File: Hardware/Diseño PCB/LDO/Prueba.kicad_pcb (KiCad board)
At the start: 2 copper layers, 54 parts, among them Q1 2N3904, Q10 BC557, Q11 BC547, Q12 BC557, Q13 2N3906, Q14 2N3904, Q15 2N3906, Q16 2N3904, Q17 2N3906, Q18 2N3904, Q19 2N3904, Q2 2N3904, Q3 2N3904, Q4 2N3906, Q5 2N3906, Q6 2N3904, Q7 2N3904, Q8 IRF4905, Q9 BC547, U1 TL431LP, U4 LM324

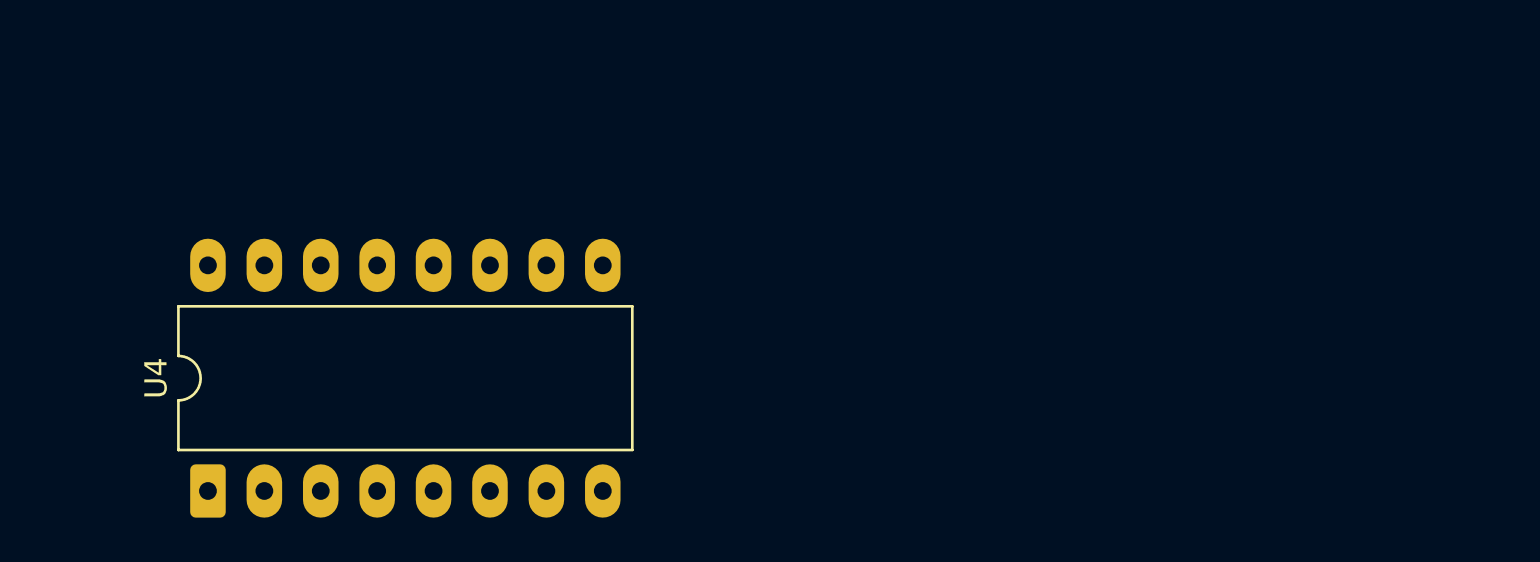
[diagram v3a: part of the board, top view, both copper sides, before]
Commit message: Diseño PCB:Arreglo LM324s con 14 pines
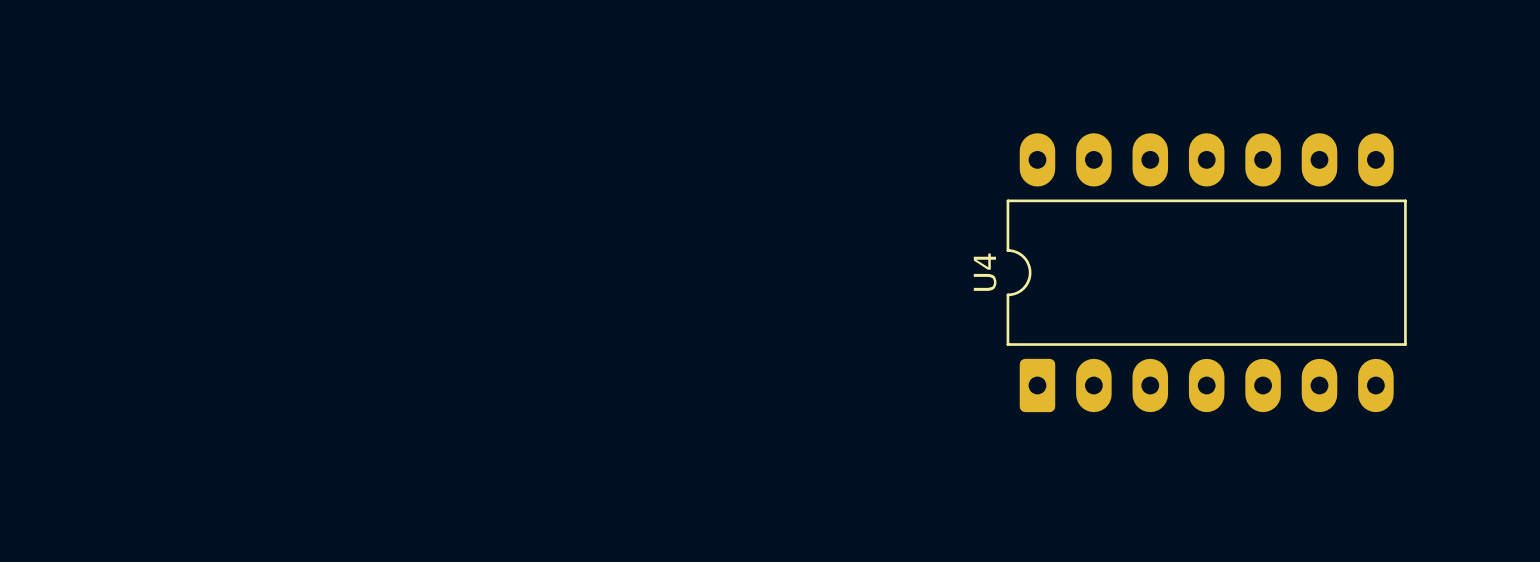
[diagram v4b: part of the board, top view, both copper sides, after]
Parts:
- U4: footprint Package_DIP:DIP-16_W10.16mm_LongPads -> Package_DIP:DIP-14_W10.16mm_LongPads
- moved U4 37.7 mm to (192.6, 102.9)
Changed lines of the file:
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@@
 		)
 	)
-	(footprint "Package_DIP:DIP-16_W10.16mm_LongPads"
+	(footprint "Package_DIP:DIP-14_W10.16mm_LongPads"
 		(layer "F.Cu")
-		(at 155.22 107.66 90)
-		(descr "16-lead though-hole mounted DIP package, row spacing 10.16mm (400 mils), LongPads")
+		(at 192.575412 102.909815 90)
+		(descr "14-lead though-hole mounted DIP package, row spacing 10.16mm (400 mils), LongPads")
 		(tags "THT DIP DIL PDIP 2.54mm 10.16mm 400mil LongPads")
 		(property "Reference" "U4"
@@
 		)
 		(property "Value" "LM324"
-			(at 5.08 20.11 90)
+			(at 5.08 17.57 90)
 			(layer "F.Fab")
 			(effects
@@
 		(fp_line
 			(start 1.845 -1.33)
-			(end 1.845 19.11)
+			(end 1.845 16.57)
 			(stroke
 				(width 0.12)
@@
 		)
 		(fp_line
-			(start 8.315 19.11)
+			(start 8.315 16.57)
 			(end 8.315 -1.33)
 			(stroke
@@
 		)
 		(fp_line
-			(start 1.845 19.11)
-			(end 8.315 19.11)
+			(start 1.845 16.57)
+			(end 8.315 16.57)
 			(stroke
 				(width 0.12)
@@
 		)
 		(fp_rect
-			(start -1.46 -1.52)
-			(end 11.61 19.3)
+			(start -1.46 -1.53)
+			(end 11.61 16.77)
 			(stroke
 				(width 0.05)
@@
 		(fp_line
 			(start 8.255 -1.27)
-			(end 8.255 19.05)
+			(end 8.255 16.51)
 			(stroke
 				(width 0.1)
@@
 		)
 		(fp_line
-			(start 8.255 19.05)
-			(end 1.905 19.05)
+			(start 8.255 16.51)
+			(end 1.905 16.51)
 			(stroke
 				(width 0.1)
@@
 		)
 		(fp_line
-			(start 1.905 19.05)
+			(start 1.905 16.51)
 			(end 1.905 -0.27)
 			(stroke
@@
 		)
 		(fp_text user "${REFERENCE}"
-			(at 5.08 8.89 0)
+			(at 5.08 7.62 180)
 			(layer "F.Fab")
 			(effects
@@
 		)
 		(point
-			(at 164.11 102.58)
+			(at 200.195412 97.829815)
 			(size 1.27)
 			(layer "F.Fab")
@@
 		)
 		(pad "8" thru_hole oval
-			(at 0 17.78 90)
+			(at 10.16 15.24 90)
 			(size 2.4 1.6)
 			(drill 0.8)
@@
 		)
 		(pad "9" thru_hole oval
-			(at 10.16 17.78 90)
+			(at 10.16 12.7 90)
 			(size 2.4 1.6)
 			(drill 0.8)
@@
 		)
 		(pad "10" thru_hole oval
-			(at 10.16 15.24 90)
+			(at 10.16 10.16 90)
 			(size 2.4 1.6)
 			(drill 0.8)
@@
 		)
 		(pad "11" thru_hole oval
-			(at 10.16 12.7 90)
+			(at 10.16 7.62 90)
 			(size 2.4 1.6)
 			(drill 0.8)
@@
 		)
 		(pad "12" thru_hole oval
-			(at 10.16 10.16 90)
+			(at 10.16 5.08 90)
 			(size 2.4 1.6)
 			(drill 0.8)
@@
 		)
 		(pad "13" thru_hole oval
-			(at 10.16 7.62 90)
+			(at 10.16 2.54 90)
 			(size 2.4 1.6)
 			(drill 0.8)
@@
 		)
 		(pad "14" thru_hole oval
-			(at 10.16 5.08 90)
+			(at 10.16 0 90)
 			(size 2.4 1.6)
 			(drill 0.8)
@@
 			(pintype "output")
 		)
-		(pad "15" thru_hole oval
-			(at 10.16 2.54 90)
-			(size 2.4 1.6)
-			(drill 0.8)
-			(layers "*.Cu" "*.Mask")
-			(remove_unused_layers no)
-		)
-		(pad "16" thru_hole oval
-			(at 10.16 0 90)
-			(size 2.4 1.6)
-			(drill 0.8)
-			(layers "*.Cu" "*.Mask")
-			(remove_unused_layers no)
-		)
 		(embedded_fonts no)
-		(model "${KICAD10_3DMODEL_DIR}/Package_DIP.3dshapes/DIP-16_W10.16mm.step"
+		(model "${KICAD10_3DMODEL_DIR}/Package_DIP.3dshapes/DIP-14_W10.16mm.step"
 			(offset
 				(xyz 0 0 0)
@@
 	(gr_poly
 		(pts
-			(xy 157.228511 105.5) (xy 158.953099 103.750185) (xy 160.728511 105.5)
+			(xy 194.275412 100.749815) (xy 196 99) (xy 197.775412 100.749815)
 		)
 		(stroke
@@
 	(gr_poly
 		(pts
-			(xy 165 105.249815) (xy 166.724588 103.5) (xy 168.5 105.249815)
+			(xy 198.275412 95) (xy 196.550824 96.749815) (xy 194.775412 95)
 		)
 		(stroke
@@
 	(gr_poly
 		(pts
-			(xy 165.724588 99.750185) (xy 164 101.5) (xy 162.224588 99.750185)
+			(xy 203.050824 100.49963) (xy 204.775412 98.749815) (xy 206.550824 100.49963)
 		)
 		(stroke
@@
 	(gr_poly
 		(pts
-			(xy 173.724588 100.250185) (xy 172 102) (xy 170.224588 100.250185)
+			(xy 206 95) (xy 204.275412 96.749815) (xy 202.5 95)
 		)
 		(stroke
@@
 		(layer "Cmts.User")
 	)
-	(gr_line
-		(start 155 103.750185)
-		(end 155 106)
+	(gr_rect
+		(start 162 62.263305)
+		(end 183 78.736694)
 		(stroke
-			(width 0.1)
-			(type default)
+			(width 0.2)
+			(type solid)
 		)
+		(fill no)
 		(layer "Cmts.User")
 	)
-	(gr_line
-		(start 158.953099 103.750185)
-		(end 155 103.750185)
+	(gr_rect
+		(start 169.509604 19.907961)
+		(end 199.351572 45.625121)
 		(stroke
-			(width 0.1)
-			(type default)
+			(width 0.2)
+			(type solid)
 		)
+		(fill no)
 		(layer "Cmts.User")
 	)
-	(gr_line
-		(start 160.5 102)
-		(end 160.5 99.5)
+	(gr_rect
+		(start 187.5 87.475256)
+		(end 224.476562 110)
 		(stroke
 			(width 0.2)
 			(type solid)
 		)
+		(fill no)
 		(layer "Cmts.User")
 	)
 	(gr_rect
-		(start 162 62.263305)
-		(end 183 78.736694)
+		(start 189 50)
+		(end 225.976562 85.024744)
 		(stroke
 			(width 0.2)
@@
 	)
 	(gr_line
-		(start 164 101.5)
-		(end 164 102)
+		(start 192.046901 99)
+		(end 192.046901 101.249815)
 		(stroke
-			(width 0.2)
-			(type solid)
+			(width 0.1)
+			(type default)
 		)
 		(layer "Cmts.User")
 	)
 	(gr_line
-		(start 164 102)
-		(end 160.5 102)
+		(start 192.275412 95.249815)
+		(end 192.275412 96.749815)
 		(stroke
-			(width 0.2)
-			(type solid)
+			(width 0.1)
+			(type default)
 		)
 		(layer "Cmts.User")
 	)
 	(gr_line
-		(start 166.724588 103.5)
-		(end 170.5 103.5)
+		(start 192.275412 96.749815)
+		(end 192.275412 95.249815)
 		(stroke
 			(width 0.1)
@@
 		(layer "Cmts.User")
 	)
-	(gr_rect
-		(start 169.509604 19.907961)
-		(end 199.351572 45.625121)
+	(gr_line
+		(start 192.275412 96.749815)
+		(end 196.550824 96.749815)
 		(stroke
-			(width 0.2)
-			(type solid)
+			(width 0.1)
+			(type default)
 		)
-		(fill no)
 		(layer "Cmts.User")
 	)
 	(gr_line
-		(start 170.5 105.5)
-		(end 170.5 103.5)
+		(start 196 99)
+		(end 192.046901 99)
 		(stroke
 			(width 0.1)
@@
 	)
 	(gr_line
-		(start 172 102)
-		(end 172 103)
+		(start 204.275412 97.249815)
+		(end 204.275412 96.749815)
 		(stroke
 			(width 0.1)
@@
 	)
 	(gr_line
-		(start 172 103)
-		(end 173 103)
+		(start 204.775412 98.749815)
+		(end 208.550824 98.749815)
 		(stroke
 			(width 0.1)
@@
 	)
 	(gr_line
-		(start 173 103)
-		(end 173 105.5)
+		(start 207.525412 97.249815)
+		(end 204.275412 97.249815)
 		(stroke
 			(width 0.1)
@@
 	)
 	(gr_line
-		(start 173 105.5)
-		(end 173 106)
+		(start 207.525412 97.249815)
+		(end 207.525412 95.249815)
 		(stroke
 			(width 0.1)
@@
 		(layer "Cmts.User")
 	)
-	(gr_rect
-		(start 189 50)
-		(end 225.976562 85.024744)
+	(gr_line
+		(start 208.550824 100.749815)
+		(end 208.550824 98.749815)
 		(stroke
-			(width 0.2)
-			(type solid)
+			(width 0.1)
+			(type default)
 		)
-		(fill no)
 		(layer "Cmts.User")
 	)
@@
 		)
 	)
-	(gr_text "Amplificadores Operacionales"
-		(at 154.5 113 0)
+	(gr_text "Lazo Tensión\n"
+		(at 166.5 74.236694 0)
 		(layer "Cmts.User")
 		(effects
@@
 		)
 	)
-	(gr_text "Lazo Tensión\n"
-		(at 166.5 74.236694 0)
+	(gr_text "Ampli. aC\n"
+		(at 171 24.5 0)
 		(layer "Cmts.User")
 		(effects
@@
 		)
 	)
-	(gr_text "Ampli. aC\n"
-		(at 171 24.5 0)
+	(gr_text "Amplificadores Operacionales"
+		(at 189.275412 108.249815 0)
 		(layer "Cmts.User")
 		(effects

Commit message: Diseño PCB
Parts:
- moved R5 91.2 mm to (84.4, 25.2)
- moved R6 91.2 mm to (84.6, 21.0)
- moved V_current_test1 66.3 mm to (109.0, 98.0)
- moved GND1 66.3 mm to (81.9, 98.0)
- moved V_Rs_test1 66.3 mm to (115.4, 98.0), turned to 180 degrees
- moved V_ref_c_test1 66.3 mm to (96.9, 97.5)
- moved V_ref_test1 66.3 mm to (90.4, 97.5)
- moved V_voltage_test1 66.3 mm to (102.4, 98.0)
- moved Q8 59.4 mm to (190.9, 40.4)
- moved U4 57.8 mm to (135.0, 97.9)
- moved Vo1 55.8 mm to (193.8, 95.8), turned to 90 degrees
- moved Q9 43.7 mm to (160.9, 69.0)
- moved Q10 43.7 mm to (152.5, 55.0)
- moved Q11 43.7 mm to (152.5, 62.0)
- moved Q12 43.7 mm to (152.5, 69.0)
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
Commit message: Diseño PCB
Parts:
- moved R2 4.05 mm to (85.0, 51.0)
- moved Q1 3.77 mm to (85.0, 46.3)
- moved R1 0.77 mm to (90.9, 41.2)
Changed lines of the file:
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@@
 	(footprint "Resistor_THT:R_Axial_DIN0204_L3.6mm_D1.6mm_P7.62mm_Horizontal"
 		(layer "F.Cu")
-		(at 90.948281 40.42 -90)
+		(at 90.948281 41.19 -90)
 		(descr "Resistor, Axial_DIN0204 series, Axial, Horizontal, pin pitch=7.62mm, 0.167W, length*diameter=3.6*1.6mm^2, http://cdn-reichelt.de/documents/datenblatt/B400/1_4W%23YAG.pdf")
 		(tags "Resistor Axial_DIN0204 series Axial Horizontal pin pitch 7.62mm 0.167W length 3.6mm diameter 1.6mm")
@@
 	(footprint "Resistor_THT:R_Axial_DIN0204_L3.6mm_D1.6mm_P7.62mm_Horizontal"
 		(layer "F.Cu")
-		(at 80.948281 51 -90)
+		(at 85 51 -90)
 		(descr "Resistor, Axial_DIN0204 series, Axial, Horizontal, pin pitch=7.62mm, 0.167W, length*diameter=3.6*1.6mm^2, http://cdn-reichelt.de/documents/datenblatt/B400/1_4W%23YAG.pdf")
 		(tags "Resistor Axial_DIN0204 series Axial Horizontal pin pitch 7.62mm 0.167W length 3.6mm diameter 1.6mm")
@@
 	(footprint "Package_TO_SOT_THT:TO-92_Inline"
 		(layer "F.Cu")
-		(at 81.308281 45.5 90)
+		(at 85 46.27 90)
 		(descr "TO-92 leads in-line, narrow, oval pads, drill 0.75mm (see NXP sot054_po.pdf)")
 		(tags "to-92 sc-43 sc-43a sot54 PA33 transistor")

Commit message: PCB: Diseño
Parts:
- added V_in1: Vin, Connector_PinHeader_2.00mm:PinHeader_1x02_P2.00mm_Vertical, F.Cu at (76.5, 108.5)
- moved Q16 71.8 mm to (128.3, 95.0), turned to 90 degrees
- moved Q15 67.4 mm to (128.3, 86.2), turned to 90 degrees
- moved Q17 65.1 mm to (128.3, 77.3), turned to 90 degrees
- moved Q14 58.0 mm to (137.0, 90.5), turned to 90 degrees
- moved Q18 53.9 mm to (137.0, 81.5), turned to 90 degrees
- moved Q19 49.2 mm to (162.5, 92.5)
- moved Q13 49.2 mm to (155.7, 92.5)
- moved Q8 42.6 mm to (164.0, 73.4)
- moved Vo1 33.5 mm to (162.2, 106.7), turned to 0 degrees
- moved R5 33.2 mm to (116.0, 35.4)
- moved R6 33.2 mm to (116.2, 31.2)
- moved R13 32.6 mm to (146.0, 43.0)
- moved R3 32.6 mm to (140.4, 30.1)
- moved R4 32.6 mm to (140.5, 43.0)
- moved Q3 29.1 mm to (153.0, 35.0)
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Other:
- board outline added: 100 x 100 mm
- board text added: "Entrada"
- board text added: "OPAMS"
- board text removed: "Amplificadores Operacionales"

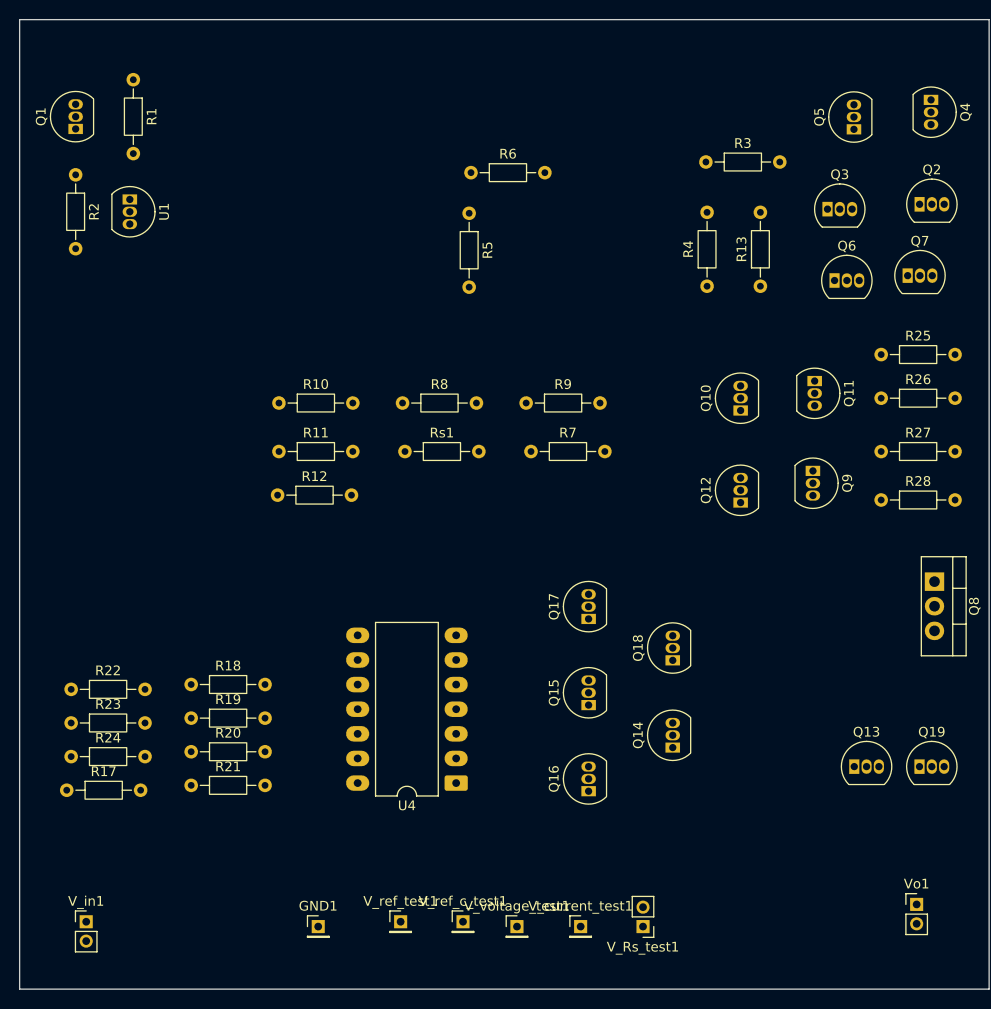
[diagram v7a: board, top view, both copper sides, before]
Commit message: Diseño PCB : Bloque testeos y Vref_t
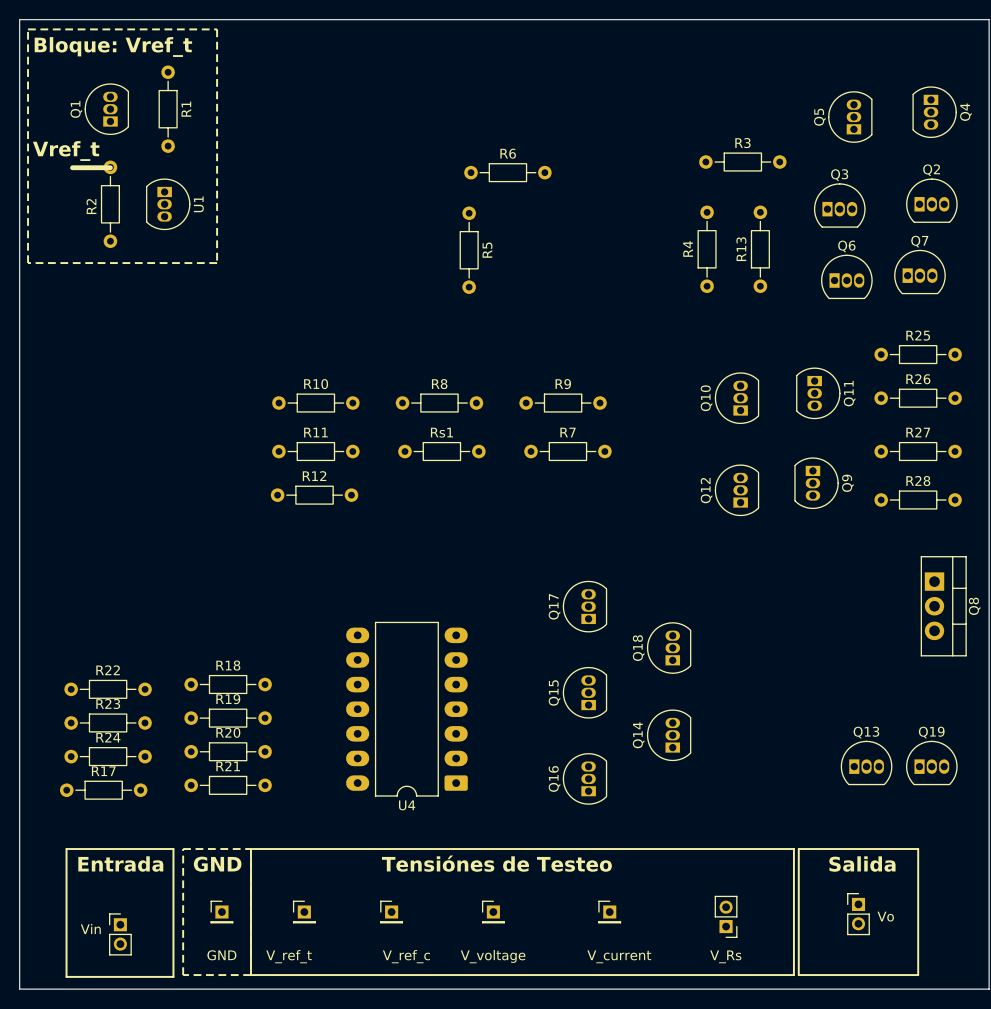
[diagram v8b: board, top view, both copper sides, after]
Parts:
- moved GND 10.0 mm to (90.5, 107.5)
- moved V_ref_t 9.98 mm to (99.0, 107.5)
- moved V_Rs 8.57 mm to (142.5, 109.0)
- moved V_ref_c 7.43 mm to (108.0, 107.5)
- moved Vo 6.00 mm to (156.2, 106.7)
- moved U1 3.67 mm to (84.6, 33.2)
- moved Q1 3.67 mm to (79.0, 26.0)
- moved R1 3.67 mm to (84.9, 20.9)
- moved R2 3.67 mm to (79.0, 30.7)
- moved Vin 3.54 mm to (80.0, 108.8)
- moved V_current 3.35 mm to (130.5, 107.5)
- moved V_voltage 2.86 mm to (118.5, 107.5)
- renumbered GND1 to GND, V_Rs_test1 to V_Rs, V_current_test1 to V_current, V_ref_c_test1 to V_ref_c, V_ref_test1 to V_ref_t, V_voltage_test1 to V_voltage, V_in1 to Vin, Vo1 to Vo
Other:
- board text added: "Bloque: Vref_t"
- board text added: "Tensiónes de Testeo"
- board text added: "Vref_t"
- board text removed: "Ref. Vref_t"
- board text removed: "Tensiónes de Test"
- board text removed: "V_ref_C"
- board text removed: "V_ref_t"
- board text removed: "Vcurrent"
- board text removed: "Vrs"
- board text removed: "Vvoltage"
